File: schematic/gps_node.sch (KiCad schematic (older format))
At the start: 75 parts, among them IC1 MMA8452Q, IC2 MCP73831/2, J1 USB_OTG, J2 AVR ICSP, J3 LIPO_BAT, J4 SOLAR, J5 FW_UPDATE, J6 SMA, Q1 Q_PMOS_GSD, SW1 SW_SP3T, SW2 RESET, U1 TLV71333PDBV, U2 ublox-cam-m8q-0, U3 ATMEGA32U4-AU, U4 RN2483, Y1 16MHz

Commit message: Schematic updated
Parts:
- removed Q1: Q_PMOS_GSD, symbol Q_PMOS_GSD
- added J17: GPIO_0, Pin_Headers:Pin_Header_Straight_1x02_Pitch2.54mm_SMD_Pin1Left, symbol Conn_01x02
- added J18: GPIO_1, Pin_Headers:Pin_Header_Straight_1x02_Pitch2.54mm_SMD_Pin1Left, symbol Conn_01x02
- added R22, R23: 4.7k, Resistors_SMD:R_0805, symbol R
- D6, D7, D8: footprint (none) -> LEDs:LED_0805
- J10, J7, J8, J9: renamed from J?; footprint (none) -> Mounting_Holes:MountingHole_3.2mm_M3_ISO14580_Pad
- J11: renamed from J?; value Conn_01x01 -> TEST Vbatt; footprint (none) -> Socket_Strips:Socket_Strip_Straight_1x01_Pitch2.54mm
- J12: renamed from J?; value Conn_01x01 -> Test 3.3v; footprint (none) -> Socket_Strips:Socket_Strip_Straight_1x01_Pitch2.54mm
- J13: renamed from J?; value Conn_01x01 -> Test Gnd; footprint (none) -> Socket_Strips:Socket_Strip_Straight_1x01_Pitch2.54mm
- J14: renamed from J?; value Conn_01x03 -> UART RF; footprint (none) -> Pin_Headers:Pin_Header_Straight_1x03_Pitch2.54mm_SMD_Pin1Left
- J15: renamed from J?; value Conn_01x03 -> I2C GPS; footprint (none) -> Pin_Headers:Pin_Header_Straight_1x03_Pitch2.54mm_SMD_Pin1Left
- J16: renamed from J?; value Conn_01x03 -> UART GPS; footprint (none) -> Pin_Headers:Pin_Header_Straight_1x03_Pitch2.54mm_SMD_Pin1Left
- R1, R10, R11, R12, R13, R14, R15, R16, R17, R18, R19, R2, R20, R21, R3, R4, R5, R6, R7, R8, R9: footprint (none) -> Resistors_SMD:R_0805
- SW1: footprint (none) -> Buttons_Switches_THT:SW_DIP_x2_W7.62mm_Slide
- U3: footprint TQFP44 -> (none)
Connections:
- net labels added: IN_0, IN_1, REG_ENABLE
- wire segments 228 -> 233
- no-connect marks 55 -> 52

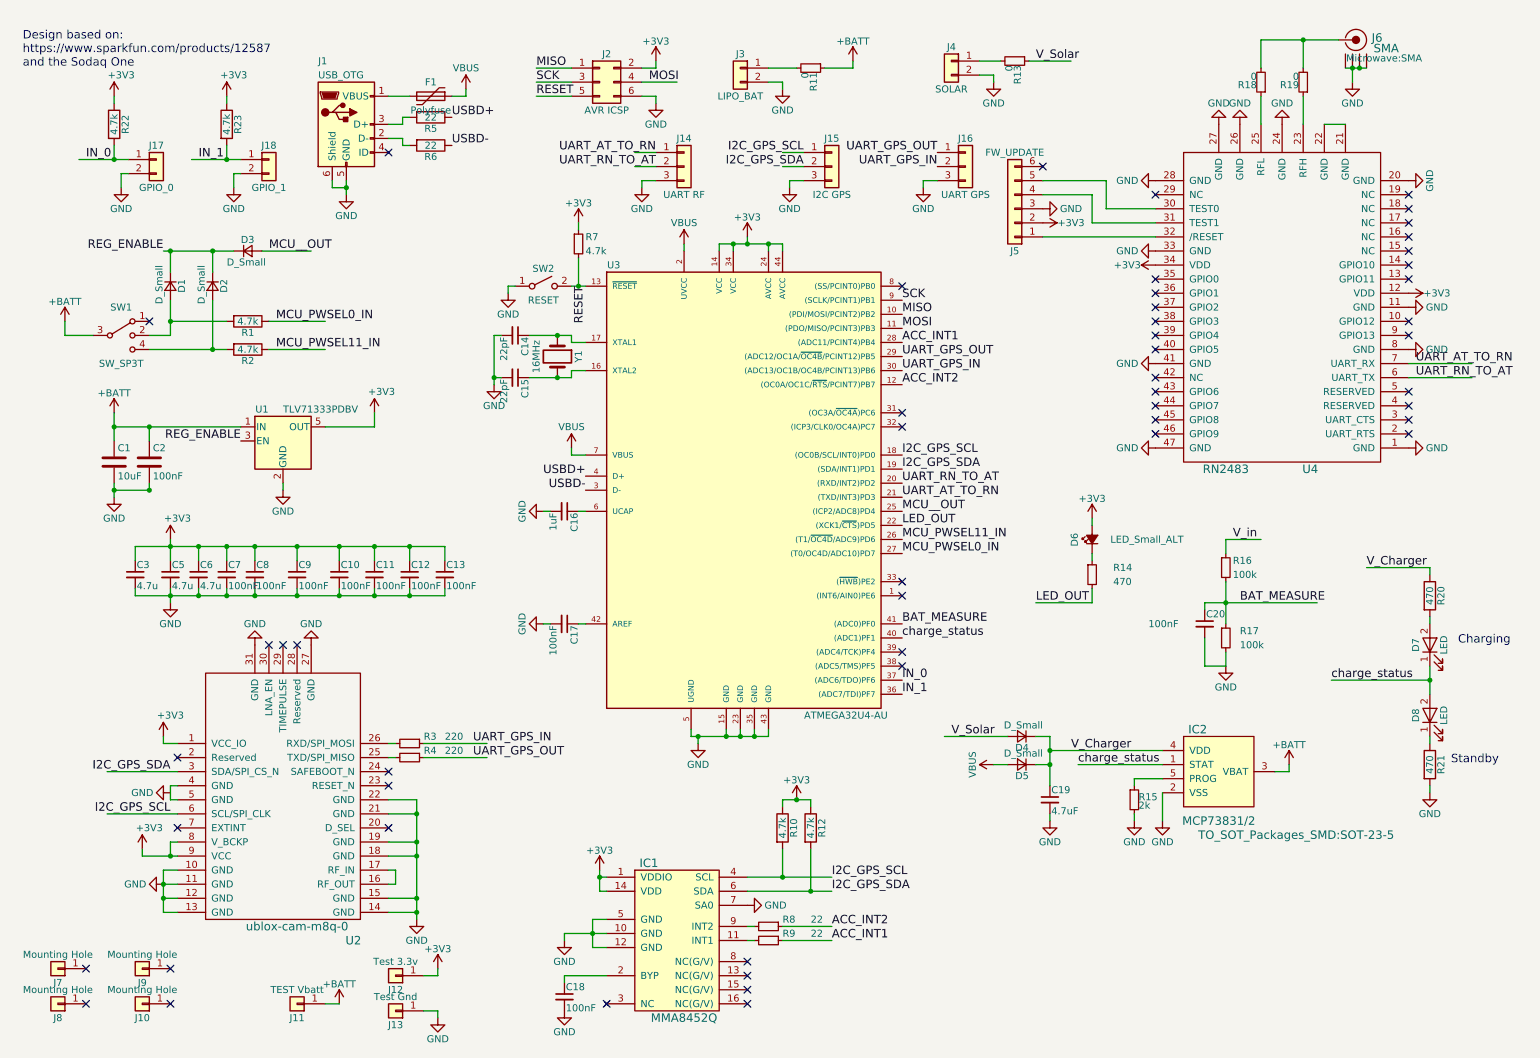
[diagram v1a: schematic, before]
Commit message: Footprints almost done, starting pcb layout
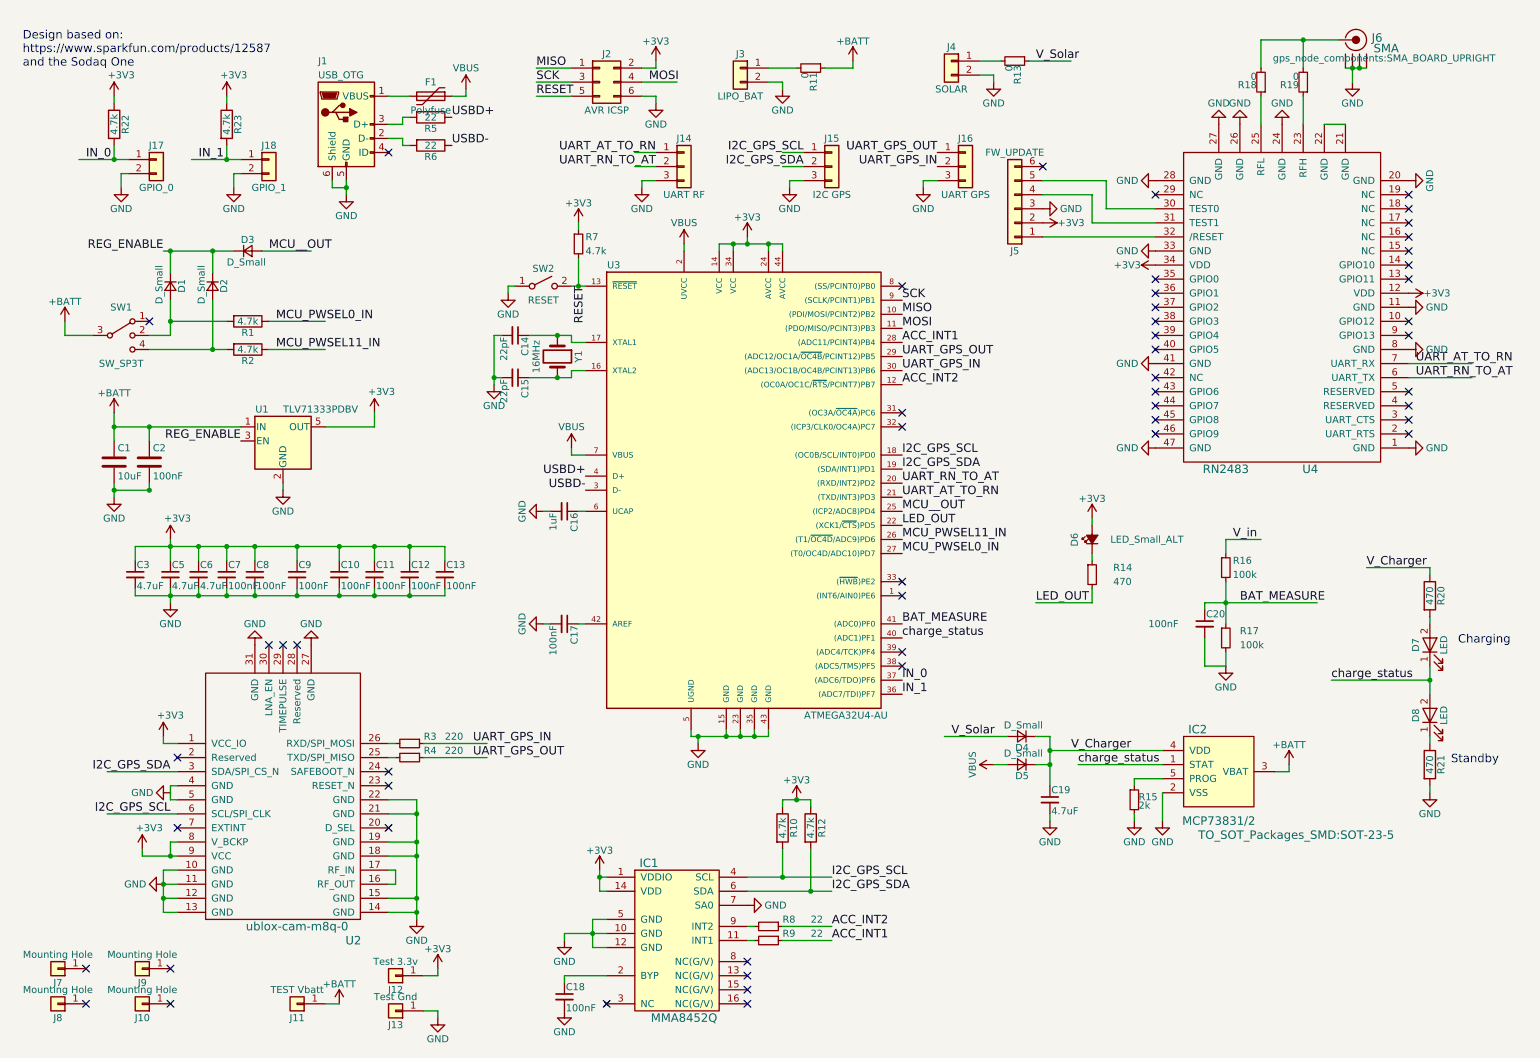
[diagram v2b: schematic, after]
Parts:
- C1: footprint Capacitors_SMD:C_0805 -> Capacitors_SMD:C_1206
- C3, C5, C6: value 4.7u -> 4.7uF
- D1, D2, D3: footprint (none) -> gps_node_components:BAS70
- D4, D5: footprint (none) -> gps_node_components:DB2J411
- F1: footprint (none) -> gps_node_components:bourns polyfuse
- J1: footprint (none) -> gps_node_components:Molex_Microusb
- J14, J15, J16: footprint Pin_Headers:Pin_Header_Straight_1x03_Pitch2.54mm_SMD_Pin1Left -> Pin_Headers:Pin_Header_Straight_1x03_Pitch2.54mm
- J17, J18: footprint Pin_Headers:Pin_Header_Straight_1x02_Pitch2.54mm_SMD_Pin1Left -> Pin_Headers:Pin_Header_Straight_1x02_Pitch2.54mm
- J2: footprint (none) -> Pin_Headers:Pin_Header_Straight_2x03_Pitch2.54mm
- J3, J4: footprint (none) -> Pin_Headers:Pin_Header_Straight_1x02_Pitch2.54mm
- J5: footprint (none) -> Pin_Headers:Pin_Header_Straight_1x06_Pitch2.54mm
- J6: footprint Microwave:SMA -> gps_node_components:SMA_BOARD_UPRIGHT
- SW1: footprint Buttons_Switches_THT:SW_DIP_x2_W7.62mm_Slide -> gps_node_components:DP3T_switch
- SW2: footprint (none) -> Buttons_Switches_SMD:SW_SPST_PTS645
- U2: footprint (none) -> drawn_by_jpmeijers:ublox-cam-m8q-0
- U3: footprint (none) -> Housings_QFP:TQFP-44_10x10mm_Pitch0.8mm
- U4: footprint (none) -> drawn_by_jpmeijers:RN2483
- Y1: footprint (none) -> gps_node_components:QC3CA_16MHz
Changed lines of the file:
@@
 F 0 "J1" H 2650 1650 50  0000 L CNN
 F 1 "USB_OTG" H 2650 1550 50  0000 L CNN
-F 2 "" H 3000 1150 50  0001 C CNN
+F 2 "gps_node_components:Molex_Microusb" H 3000 1150 50  0001 C CNN
 F 3 "" H 3000 1150 50  0001 C CNN
 	1    2850 1200
@@
 F 0 "F1" V 3350 1000 50  0000 C CNN
 F 1 "Polyfuse" V 3550 1000 50  0000 C CNN
-F 2 "" H 3500 800 50  0001 L CNN
+F 2 "gps_node_components:bourns polyfuse" H 3500 800 50  0001 L CNN
 F 3 "" H 3450 1000 50  0001 C CNN
 	1    3450 1000
@@
 F 0 "D5" H 7600 5830 50  0000 L CNN
 F 1 "D_Small" H 7500 5670 50  0000 L CNN
-F 2 "" V 7650 5750 50  0001 C CNN
+F 2 "gps_node_components:DB2J411" V 7650 5750 50  0001 C CNN
 F 3 "" V 7650 5750 50  0001 C CNN
 	1    7650 5750
@@
 F 0 "D4" H 7600 5630 50  0000 L CNN
 F 1 "D_Small" H 7500 5470 50  0000 L CNN
-F 2 "" V 7650 5550 50  0001 C CNN
+F 2 "gps_node_components:DB2J411" V 7650 5550 50  0001 C CNN
 F 3 "" V 7650 5550 50  0001 C CNN
 	1    7650 5550
@@
 F 0 "U4" H 9700 750 60  0000 C CNN
 F 1 "RN2483" H 9100 750 60  0000 C CNN
-F 2 "" H 9600 1500 60  0001 C CNN
+F 2 "drawn_by_jpmeijers:RN2483" H 9600 1500 60  0001 C CNN
 F 3 "" H 9600 1500 60  0000 C CNN
 	1    9500 2200
@@
 F 0 "J6" H 10175 1215 60  0000 C CNN
 F 1 "SMA" H 10240 1140 60  0000 C CNN
-F 2 "Microwave:SMA" H 10225 1070 50  0000 C CNN
+F 2 "gps_node_components:SMA_BOARD_UPRIGHT" H 10225 1070 50  0000 C CNN
 F 3 "" H 10050 900 60  0000 C CNN
 	1    10050 900
@@
 F 0 "Y1" H 4350 3000 50  0000 C CNN
 F 1 "16MHz" H 4350 2700 50  0000 C CNN
-F 2 "" H 4350 2850 50  0001 C CNN
+F 2 "gps_node_components:QC3CA_16MHz" H 4350 2850 50  0001 C CNN
 F 3 "" H 4350 2850 50  0001 C CNN
 	1    4350 2850
@@
 F 0 "J5" H 7600 2100 50  0000 C CNN
 F 1 "FW_UPDATE" H 7600 1400 50  0000 C CNN
-F 2 "" H 7600 1800 50  0001 C CNN
+F 2 "Pin_Headers:Pin_Header_Straight_1x06_Pitch2.54mm" H 7600 1800 50  0001 C CNN
 F 3 "" H 7600 1800 50  0001 C CNN
 	1    7600 1800
@@
 F 0 "SW2" H 4250 2475 50  0000 C CNN
 F 1 "RESET" H 4250 2250 50  0000 C CNN
-F 2 "" H 4250 2350 50  0001 C CNN
+F 2 "Buttons_Switches_SMD:SW_SPST_PTS645" H 4250 2350 50  0001 C CNN
 F 3 "" H 4250 2350 50  0001 C CNN
 	1    4250 2350
@@
 F 0 "U2" H 1900 7000 60  0000 C CNN
 F 1 "ublox-cam-m8q-0" H 2300 6900 60  0000 C CNN
-F 2 "" H 2400 7100 60  0001 C CNN
+F 2 "drawn_by_jpmeijers:ublox-cam-m8q-0" H 2400 7100 60  0001 C CNN
 F 3 "" H 2400 7100 60  0001 C CNN
 	1    2400 6100
@@
 F 0 "J3" H 5650 900 50  0000 C CNN
 F 1 "LIPO_BAT" H 5650 600 50  0000 C CNN
-F 2 "" H 5650 800 50  0001 C CNN
+F 2 "Pin_Headers:Pin_Header_Straight_1x02_Pitch2.54mm" H 5650 800 50  0001 C CNN
 F 3 "" H 5650 800 50  0001 C CNN
 	1    5650 800
@@
 F 0 "J4" H 7150 850 50  0000 C CNN
 F 1 "SOLAR" H 7150 550 50  0000 C CNN
-F 2 "" H 7150 750 50  0001 C CNN
+F 2 "Pin_Headers:Pin_Header_Straight_1x02_Pitch2.54mm" H 7150 750 50  0001 C CNN
 F 3 "" H 7150 750 50  0001 C CNN
 	1    7150 750
@@
 F 0 "J2" H 4700 1100 50  0000 C CNN
 F 1 "AVR ICSP" H 4700 700 50  0000 C CNN
-F 2 "" H 4650 900 50  0001 C CNN
+F 2 "Pin_Headers:Pin_Header_Straight_2x03_Pitch2.54mm" H 4650 900 50  0001 C CNN
 F 3 "" H 4650 900 50  0001 C CNN
 	1    4650 900
@@
 F 0 "SW1" H 1250 2900 50  0000 C CNN
 F 1 "SW_SP3T" H 1250 2500 50  0000 C CNN
-F 2 "Buttons_Switches_THT:SW_DIP_x2_W7.62mm_Slide" H 625 2875 50  0001 C CNN
+F 2 "gps_node_components:DP3T_switch" H 625 2875 50  0001 C CNN
 F 3 "" H 625 2875 50  0001 C CNN
 	1    1250 2700
@@
 F 0 "C1" H 1225 3700 50  0000 L CNN
 F 1 "10uF" H 1225 3500 50  0000 L CNN
-F 2 "Capacitors_SMD:C_0805" H 1238 3450 50  0001 C CNN
+F 2 "Capacitors_SMD:C_1206" H 1238 3450 50  0001 C CNN
 F 3 "" H 1200 3600 50  0001 C CNN
 	1    1200 3600
@@
 P 1600 4400
 F 0 "C5" H 1610 4470 50  0000 L CNN
-F 1 "4.7u" H 1610 4320 50  0000 L CNN
+F 1 "4.7uF" H 1610 4320 50  0000 L CNN
 F 2 "Capacitors_SMD:C_0805" H 1600 4400 50  0001 C CNN
 F 3 "" H 1600 4400 50  0001 C CNN
@@
 P 1800 4400
 F 0 "C6" H 1810 4470 50  0000 L CNN
-F 1 "4.7u" H 1810 4320 50  0000 L CNN
+F 1 "4.7uF" H 1810 4320 50  0000 L CNN
 F 2 "Capacitors_SMD:C_0805" H 1800 4400 50  0001 C CNN
 F 3 "" H 1800 4400 50  0001 C CNN
@@
 F 0 "D2" H 1850 2430 50  0000 L CNN
 F 1 "D_Small" H 1750 2270 50  0000 L CNN
-F 2 "" V 1900 2350 50  0001 C CNN
+F 2 "gps_node_components:BAS70" V 1900 2350 50  0001 C CNN
 F 3 "" V 1900 2350 50  0001 C CNN
 	1    1900 2350
@@
 F 0 "D1" H 1550 2430 50  0000 L CNN
 F 1 "D_Small" H 1450 2270 50  0000 L CNN
-F 2 "" V 1600 2350 50  0001 C CNN
+F 2 "gps_node_components:BAS70" V 1600 2350 50  0001 C CNN
 F 3 "" V 1600 2350 50  0001 C CNN
 	1    1600 2350
@@
 F 0 "D3" H 2100 2180 50  0000 L CNN
 F 1 "D_Small" H 2000 2020 50  0000 L CNN
-F 2 "" V 2150 2100 50  0001 C CNN
+F 2 "gps_node_components:BAS70" V 2150 2100 50  0001 C CNN
 F 3 "" V 2150 2100 50  0001 C CNN
 	1    2150 2100
@@
 P 1350 4400
 F 0 "C3" H 1360 4470 50  0000 L CNN
-F 1 "4.7u" H 1360 4320 50  0000 L CNN
+F 1 "4.7uF" H 1360 4320 50  0000 L CNN
 F 2 "Capacitors_SMD:C_0805" H 1350 4400 50  0001 C CNN
 F 3 "" H 1350 4400 50  0001 C CNN
@@
 F 0 "J14" H 5250 1700 50  0000 C CNN
 F 1 "UART RF" H 5250 1300 50  0000 C CNN
-F 2 "Pin_Headers:Pin_Header_Straight_1x03_Pitch2.54mm_SMD_Pin1Left" H 5250 1500 50  0001 C CNN
+F 2 "Pin_Headers:Pin_Header_Straight_1x03_Pitch2.54mm" H 5250 1500 50  0001 C CNN
 F 3 "" H 5250 1500 50  0001 C CNN
 	1    5250 1500
@@
 F 0 "J15" H 6300 1700 50  0000 C CNN
 F 1 "I2C GPS" H 6300 1300 50  0000 C CNN
-F 2 "Pin_Headers:Pin_Header_Straight_1x03_Pitch2.54mm_SMD_Pin1Left" H 6300 1500 50  0001 C CNN
+F 2 "Pin_Headers:Pin_Header_Straight_1x03_Pitch2.54mm" H 6300 1500 50  0001 C CNN
 F 3 "" H 6300 1500 50  0001 C CNN
 	1    6300 1500
@@
 F 0 "J16" H 7250 1700 50  0000 C CNN
 F 1 "UART GPS" H 7250 1300 50  0000 C CNN
-F 2 "Pin_Headers:Pin_Header_Straight_1x03_Pitch2.54mm_SMD_Pin1Left" H 7250 1500 50  0001 C CNN
+F 2 "Pin_Headers:Pin_Header_Straight_1x03_Pitch2.54mm" H 7250 1500 50  0001 C CNN
 F 3 "" H 7250 1500 50  0001 C CNN
 	1    7250 1500
@@
 F 0 "J17" H 1500 1550 50  0000 C CNN
 F 1 "GPIO_0" H 1500 1250 50  0000 C CNN
-F 2 "Pin_Headers:Pin_Header_Straight_1x02_Pitch2.54mm_SMD_Pin1Left" H 1500 1450 50  0001 C CNN
+F 2 "Pin_Headers:Pin_Header_Straight_1x02_Pitch2.54mm" H 1500 1450 50  0001 C CNN
 F 3 "" H 1500 1450 50  0001 C CNN
 	1    1500 1450
@@
 F 0 "U3" H 4750 5600 50  0000 C CNN
 F 1 "ATMEGA32U4-AU" H 6400 2400 50  0000 C CNN
-F 2 "" H 5700 3900 50  0001 C CIN
+F 2 "Housings_QFP:TQFP-44_10x10mm_Pitch0.8mm" H 5700 3900 50  0001 C CIN
 F 3 "" H 6800 5000 50  0001 C CNN
 	1    5700 3900
@@
 F 0 "J18" H 2300 1550 50  0000 C CNN
 F 1 "GPIO_1" H 2300 1250 50  0000 C CNN
-F 2 "Pin_Headers:Pin_Header_Straight_1x02_Pitch2.54mm_SMD_Pin1Left" H 2300 1450 50  0001 C CNN
+F 2 "Pin_Headers:Pin_Header_Straight_1x02_Pitch2.54mm" H 2300 1450 50  0001 C CNN
 F 3 "" H 2300 1450 50  0001 C CNN
 	1    2300 1450

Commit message: First round of layout done
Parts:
- IC1: footprint (none) -> gps_node_components:MMA8452Q
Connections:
- net labels removed: V_in
- wire segments 233 -> 231
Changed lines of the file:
@@
 F 0 "IC1" H 5000 7550 60  0000 C CNN
 F 1 "MMA8452Q" H 5250 6450 60  0000 C CNN
-F 2 "" H 5200 7000 60  0001 C CNN
+F 2 "gps_node_components:MMA8452Q" H 5200 7000 60  0001 C CNN
 F 3 "" H 5200 7000 60  0000 C CNN
 	1    5200 7000
@@
 	1    0    0    -1
 $EndComp
-Text Label 9150 4150 0    60   ~ 0
-V_in
 Text Label 6800 4050 0    60   ~ 0
 LED_OUT
@@
 	9550 5800 9550 5750
 Wire Wire Line
-	9800 1200 9950 1200
-Wire Wire Line
 	9950 800  10100 800
 Connection ~ 10000 800
@@
 	4550 2750 4450 2750
 Wire Wire Line
-	4450 2750 4450 2700
-Wire Wire Line
-	4450 2700 4150 2700
+	4450 2700 4450 2750
+Wire Wire Line
+	4150 2700 4450 2700
 Connection ~ 4350 2700
 Wire Wire Line
 	4550 2950 4450 2950
 Wire Wire Line
-	4450 2950 4450 3000
-Wire Wire Line
-	4450 3000 4150 3000
+	4450 3000 4450 2950
+Wire Wire Line
+	4150 3000 4450 3000
 Connection ~ 4350 3000
 Wire Wire Line
@@
 Wire Wire Line
 	850  2700 850  2600
-Wire Wire Line
-	9100 4150 9350 4150
 Wire Wire Line
 	7750 4600 8150 4600
@@
 Text Label 1800 1450 0    60   ~ 0
 IN_1
+$Comp
+L +BATT #PWR070
+U 1 1 5A7749B5
+P 9100 4150
+F 0 "#PWR070" H 9100 4000 50  0001 C CNN
+F 1 "+BATT" H 9100 4290 50  0000 C CNN
+F 2 "" H 9100 4150 50  0001 C CNN
+F 3 "" H 9100 4150 50  0001 C CNN
+	1    9100 4150
+	1    0    0    -1
+$EndComp
+$Comp
+L GND #PWR071
+U 1 1 5A7778D3
+P 9800 1200
+F 0 "#PWR071" H 9800 950 50  0001 C CNN
+F 1 "GND" H 9800 1050 50  0000 C CNN
+F 2 "" H 9800 1200 50  0001 C CNN
+F 3 "" H 9800 1200 50  0001 C CNN
+	1    9800 1200
+	-1   0    0    1
+$EndComp
+$Comp
+L GND #PWR072
+U 1 1 5A7779C8
+P 9950 1200
+F 0 "#PWR072" H 9950 950 50  0001 C CNN
+F 1 "GND" H 9950 1050 50  0000 C CNN
+F 2 "" H 9950 1200 50  0001 C CNN
+F 3 "" H 9950 1200 50  0001 C CNN
+	1    9950 1200
+	-1   0    0    1
+$EndComp
 $EndSCHEMATC
